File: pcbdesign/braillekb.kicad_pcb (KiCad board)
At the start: 2 copper layers, 97 x 69.2 mm, 32 parts, among them J1 Conn_01x08, J2 Conn_01x04, SW1 SW_Push, SW2 SW_Push, SW3 SW_Push, SW4 SW_Push, SW5 SW_Push, SW6 SW_Push

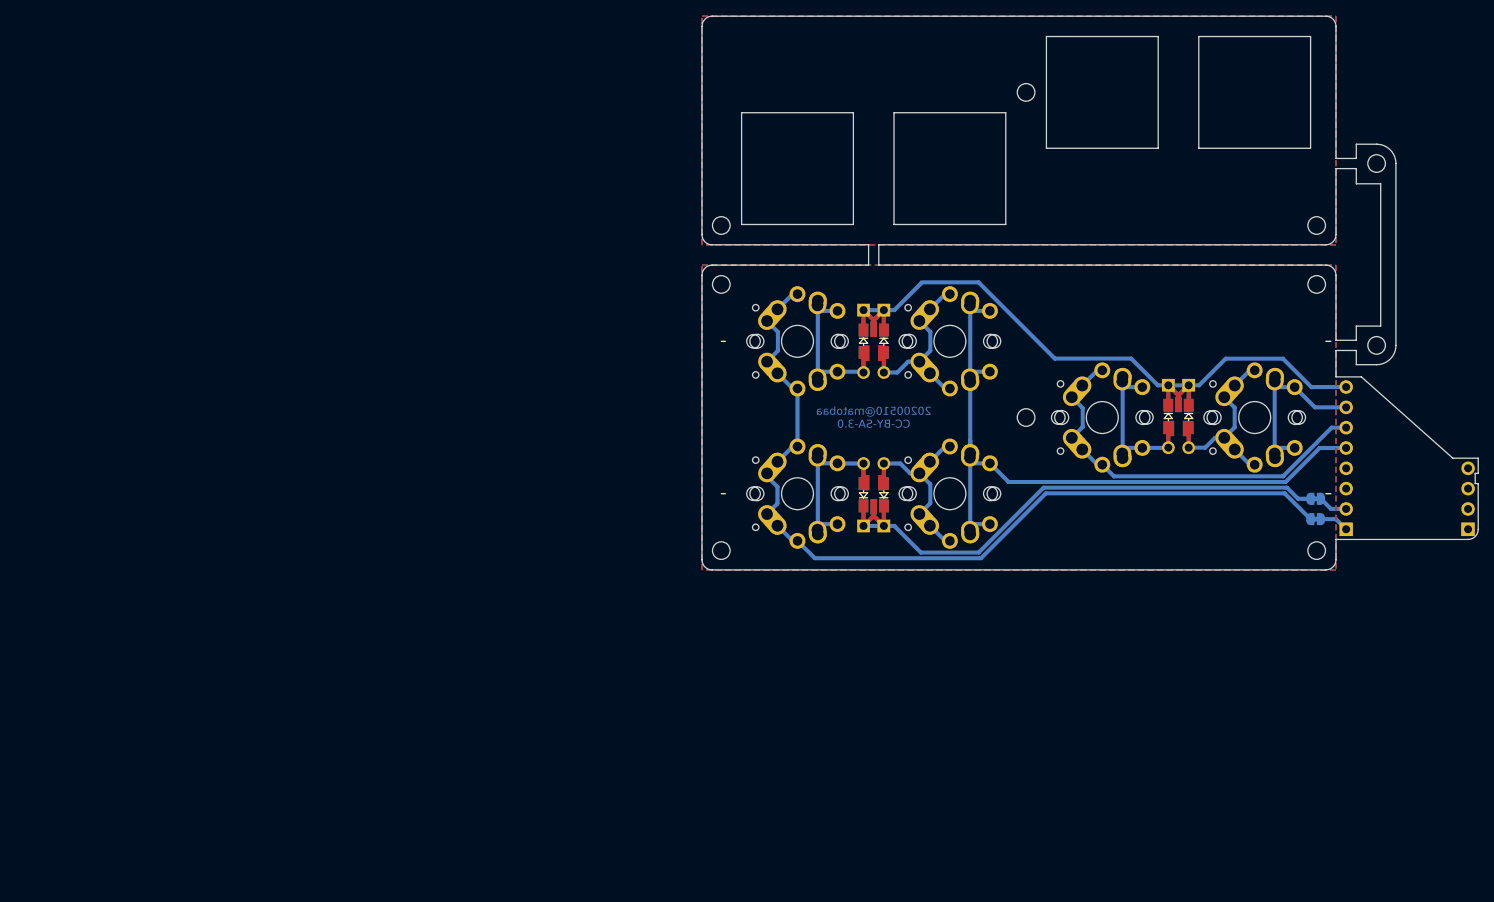
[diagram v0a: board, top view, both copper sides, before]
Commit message: 8x3 in one pcb
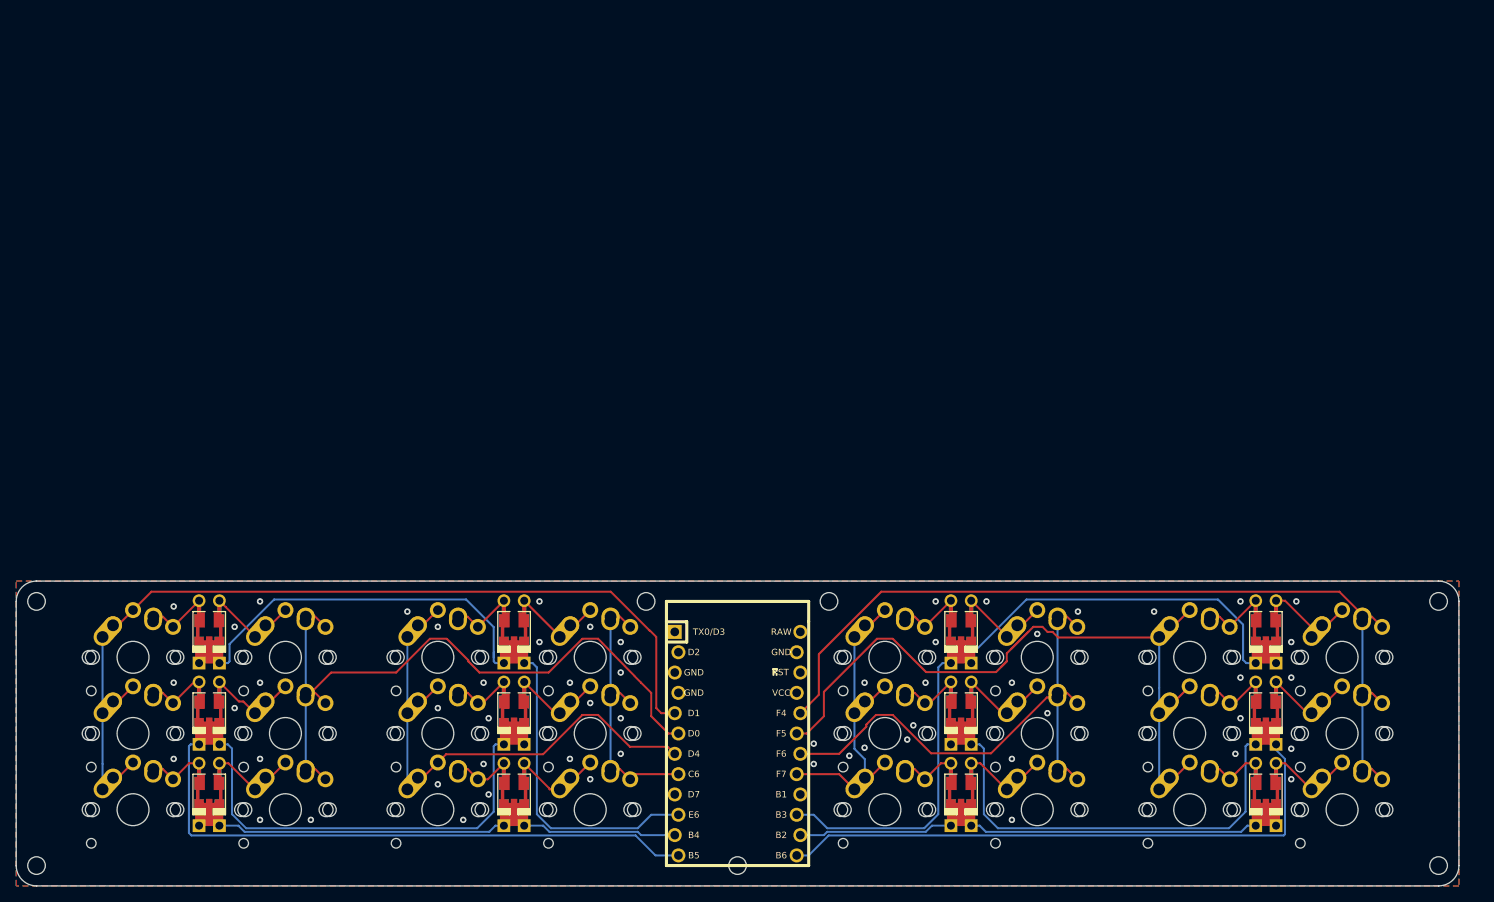
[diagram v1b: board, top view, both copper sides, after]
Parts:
- removed D1, D2, D3, D4, D5, D6: D, Keebio:Diode-dual
- removed D12, D32, D34, D43, D56, D65: KCom, library:SOT-23_Handsoldering
- removed H10, H8, H9: Pad, MountingHole:MountingHole_2.2mm_M2
- removed J1: Conn_01x08, Connector_PinHeader_2.54mm:PinHeader_1x08_P2.54mm_Vertical
- removed J2: Conn_01x04, Connector_PinHeader_2.54mm:PinHeader_1x04_P2.54mm_Vertical
- removed JP1, JP2: SolderJumper_2_Bridged, Jumper:SolderJumper-2_P1.3mm_Bridged_RoundedPad1.0x1.5mm
- removed SW1, SW2, SW3, SW4, SW5, SW6: SW_Push, library:MX-Alps-Choc-1U-reversible
- added DD11: D_KCom, local:SOT-23_dual_bridged, F.Cu at (46.4, 127.0)
- added DD13: D_KCom, local:SOT-23_dual_bridged, F.Cu at (84.5, 127.0)
- added DD21: D_KCom, local:SOT-23_dual_bridged, F.Cu at (46.4, 137.2)
- added DD23: D_KCom, local:SOT-23_dual_bridged, F.Cu at (84.5, 137.2)
- added DD31: D_KCom, local:SOT-23_dual_bridged, F.Cu at (46.4, 147.3)
- added DD33: D_KCom, local:SOT-23_dual_bridged, F.Cu at (84.5, 147.3)
- added DD45: D_KCom, local:SOT-23_dual_bridged, F.Cu at (140.3, 127.0)
- added DD47: D_KCom, local:SOT-23_dual_bridged, F.Cu at (178.4, 127.0)
- added DD55: D_KCom, local:SOT-23_dual_bridged, F.Cu at (140.3, 137.2)
- added DD57: D_KCom, local:SOT-23_dual_bridged, F.Cu at (178.4, 137.2)
- added DD65: D_KCom, local:SOT-23_dual_bridged, F.Cu at (140.3, 147.3)
- added DD67: D_KCom, local:SOT-23_dual_bridged, F.Cu at (178.4, 147.3)
- added SW11: SW_Push, Keebio:MX-Alps-Choc-1U-NoLED, F.Cu at (36.8, 130.2)
- added SW12: SW_Push, Keebio:MX-Alps-Choc-1U-NoLED, F.Cu at (55.9, 130.2)
- added SW13: SW_Push, Keebio:MX-Alps-Choc-1U-NoLED, F.Cu at (74.9, 130.2)
- added SW14: SW_Push, Keebio:MX-Alps-Choc-1U-NoLED, F.Cu at (94.0, 130.2)
- added SW21: SW_Push, Keebio:MX-Alps-Choc-1U-NoLED, F.Cu at (36.8, 139.7)
- added SW22: SW_Push, Keebio:MX-Alps-Choc-1U-NoLED, F.Cu at (55.9, 139.7)
- added SW23: SW_Push, Keebio:MX-Alps-Choc-1U-NoLED, F.Cu at (74.9, 139.7)
- added SW24: SW_Push, Keebio:MX-Alps-Choc-1U-NoLED, F.Cu at (94.0, 139.7)
- added SW31: SW_Push, Keebio:MX-Alps-Choc-1U-NoLED, F.Cu at (36.8, 149.2)
- added SW32: SW_Push, Keebio:MX-Alps-Choc-1U-NoLED, F.Cu at (55.9, 149.2)
- added SW33: SW_Push, Keebio:MX-Alps-Choc-1U-NoLED, F.Cu at (74.9, 149.2)
- added SW34: SW_Push, Keebio:MX-Alps-Choc-1U-NoLED, F.Cu at (94.0, 149.2)
- added SW45: SW_Push, Keebio:MX-Alps-Choc-1U-NoLED, F.Cu at (130.8, 130.2)
- added SW46: SW_Push, Keebio:MX-Alps-Choc-1U-NoLED, F.Cu at (149.9, 130.2)
- added SW47: SW_Push, Keebio:MX-Alps-Choc-1U-NoLED, F.Cu at (168.9, 130.2)
- added SW48: SW_Push, Keebio:MX-Alps-Choc-1U-NoLED, F.Cu at (188.0, 130.2)
- added SW55: SW_Push, Keebio:MX-Alps-Choc-1U-NoLED, F.Cu at (130.8, 139.7)
- added SW56: SW_Push, Keebio:MX-Alps-Choc-1U-NoLED, F.Cu at (149.9, 139.7)
- added SW57: SW_Push, Keebio:MX-Alps-Choc-1U-NoLED, F.Cu at (168.9, 139.7)
- added SW58: SW_Push, Keebio:MX-Alps-Choc-1U-NoLED, F.Cu at (188.0, 139.7)
- added SW65: SW_Push, Keebio:MX-Alps-Choc-1U-NoLED, F.Cu at (130.8, 149.2)
- added SW66: SW_Push, Keebio:MX-Alps-Choc-1U-NoLED, F.Cu at (149.9, 149.2)
- added SW67: SW_Push, Keebio:MX-Alps-Choc-1U-NoLED, F.Cu at (168.9, 149.2)
- added SW68: SW_Push, Keebio:MX-Alps-Choc-1U-NoLED, F.Cu at (188.0, 149.2)
- added U11: ProMicro, Keebio:ArduinoProMicro-ZigZag, F.Cu at (112.4, 141.0)
- H1, H2, H3, H4, H5, H6, H7: value Pad -> MountingHole
- moved H5 164.8 mm to (24.8, 156.2)
- moved H7 109.5 mm to (200.0, 156.2)
- moved H1 94.3 mm to (24.8, 123.2)
- moved H2 92.7 mm to (101.0, 123.2)
- moved H4 89.9 mm to (200.0, 123.2)
- moved H6 80.0 mm to (112.4, 156.2)
- moved H3 33.7 mm to (123.8, 123.2)
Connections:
- H1 pad 1: GND -> (no net)
- H2 pad 1: GND -> (no net)
- H3 pad 1: GND -> (no net)
- H4 pad 1: GND -> (no net)
- H5 pad 1: GND -> (no net)
- H6 pad 1: GND -> (no net)
- H7 pad 1: GND -> (no net)
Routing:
- net R2: track 0.00 -> 128.4 mm
- net R5: track 0.00 -> 127.7 mm
- net C1: track 0.00 -> 114.8 mm
- net C8: track 0.00 -> 109.6 mm
- net /C2: track 102.5 -> 0.00 mm
- net C7: track 0.00 -> 95.8 mm
- net /R3: track 88.7 -> 0.00 mm
- net /C3: track 88.1 -> 0.00 mm
- net C2: track 0.00 -> 88.0 mm
- net R1: track 0.00 -> 85.8 mm
- net R4: track 0.00 -> 84.6 mm
- net /R2: track 70.9 -> 0.00 mm
- net C3: track 0.00 -> 68.7 mm
- net C6: track 0.00 -> 67.2 mm
- net R3: track 0.00 -> 55.5 mm
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- added copper zone on B.Cu, net GND
- added copper zone on F.Cu, net GND
- removed copper zone on B.Cu, net (none)
- removed copper zone on F.Cu, net (none)
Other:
- board size 97 x 69.2 mm -> 180.3 x 38.1 mm
- net class Default: clearance 0.1524 -> 0.1
- rule trace_clearance: 0.1524 -> 0.1
- board text removed: "20200510@matobaa CC-BY-SA-3.0"

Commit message: simplified
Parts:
- removed DD11, DD13, DD21, DD23, DD31, DD33, DD45, DD47, DD55, DD57, DD65, DD67: D_KCom, local:SOT-23_dual_bridged
- removed SW13, SW14, SW21, SW22, SW31, SW32, SW33, SW34, SW45, SW46, SW57, SW58, SW65, SW66, SW67, SW68: SW_Push, Keebio:MX-Alps-Choc-1U-NoLED
- added H8: MountingHole, MountingHole:MountingHole_2.2mm_M2, F.Cu at (123.8, 156.2)
- moved H6 11.4 mm to (101.0, 156.2)
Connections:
- SW11 pad 1: Net-(DD11-Pad2) -> R1
- SW12 pad 2: Net-(DD11-Pad1) -> R1
- SW23 pad 1: Net-(DD23-Pad2) -> R1
- SW24 pad 2: Net-(DD23-Pad1) -> R1
- SW47 pad 1: Net-(DD47-Pad2) -> R4
- SW48 pad 2: Net-(DD47-Pad1) -> R4
- SW55 pad 1: Net-(DD55-Pad2) -> R4
- SW56 pad 2: Net-(DD55-Pad1) -> R4
- U11 pad 11: R3 -> (no net)
- U11 pad 12: R2 -> (no net)
- U11 pad 13: R5 -> (no net)
- U11 pad 14: R6 -> (no net)
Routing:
- net R2: track 128.4 -> 0.00 mm
- net R5: track 127.7 -> 0.00 mm
- net R3: track 55.5 -> 0.00 mm
- net R6: track 55.5 -> 0.00 mm
- net C7: track 95.8 -> 55.5 mm
- net R4: track 84.6 -> 120.6 mm
- net C1: track 114.8 -> 81.7 mm
- net C2: track 88.0 -> 55.9 mm
- net C8: track 109.6 -> 79.8 mm
- net R1: track 85.8 -> 113.5 mm
- net C3: track 68.7 -> 41.9 mm
- net C6: track 67.2 -> 41.4 mm
- net C5: track 41.7 -> 18.5 mm
- net C4: track 34.4 -> 18.7 mm
- net Net-(DD47-Pad1): track 12.2 -> 0.00 mm
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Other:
- board text added: "//github.com/matobaa/braille_keyboard"
- board text added: "CC-BY-SA-2.0 / rev2-simplified"
- board text added: "Copy"
- board text added: "Cut"
- board text added: "Down"
- board text added: "End"
- board text added: "Enter"
- board text added: "Home"
- board text added: "Left"
- board text added: "Paste"
- board text added: "Redo"
- board text added: "Right"
- board text added: "Shift"
- board text added: "Undo"
- board text added: "Up"
